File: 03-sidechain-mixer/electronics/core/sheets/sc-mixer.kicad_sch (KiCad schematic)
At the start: 48 parts, among them Q1 BC847BS, U1 TL072, U2 TL072, U3 TL072, U4 TL072

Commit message: Started VCF
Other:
- note added: "Pots to be moved over to the UI board"
- note added: "Pots to be moved over to the UI board. For channel 4 there can be two inputs from the UI board: one straigth from the jack (goes to peak detector), and one which is after a log volume pot control."
- note added: "Pots to be moved over to the UI board. The main volume control can happen on the UI board?"
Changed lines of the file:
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@@
+		)
+	)
+	(text "Pots to be moved over \nto the UI board.\nThe main volume control can\nhappen on the UI board?"
+		(exclude_from_sim no)
+		(at 287.02 63.5 0)
+		(effects
+			(font
+				(size 2 2)
+				(color 255 0 255 1)
+			)
+			(justify left)
 		)
 	)
@@
 			(font
 				(size 1.27 1.27)
+			)
+			(justify left)
+		)
+	)
+	(text "Pots to be moved over \nto the UI board"
+		(exclude_from_sim no)
+		(at 143.51 113.03 0)
+		(effects
+			(font
+				(size 2 2)
+				(color 255 0 255 1)
 			)
 			(justify left)
@@
 		)
 	)
+	(text "Pots to be moved over \nto the UI board.\nFor channel 4 there\ncan be two inputs from\nthe UI board: one straigth\nfrom the jack (goes to peak\ndetector), and one which is\nafter a log volume pot control.\n"
+		(exclude_from_sim no)
+		(at 40.64 186.69 0)
+		(effects
+			(font
+				(size 2 2)
+				(color 255 0 255 1)
+			)
+			(justify left)
+		)
+	)
 	(text "DC coupled input allows the mixer\nto be used for audio as well as CV"
 		(exclude_from_sim no)
@@
 			)
 			(justify left)
+		)
+	)
+	(text "Pots to be moved over \nto the UI board"
+		(exclude_from_sim no)
+		(at -7.62 55.88 0)
+		(effects
+			(font
+				(size 2 2)
+				(color 255 0 255 1)
+			)
+			(justify left)

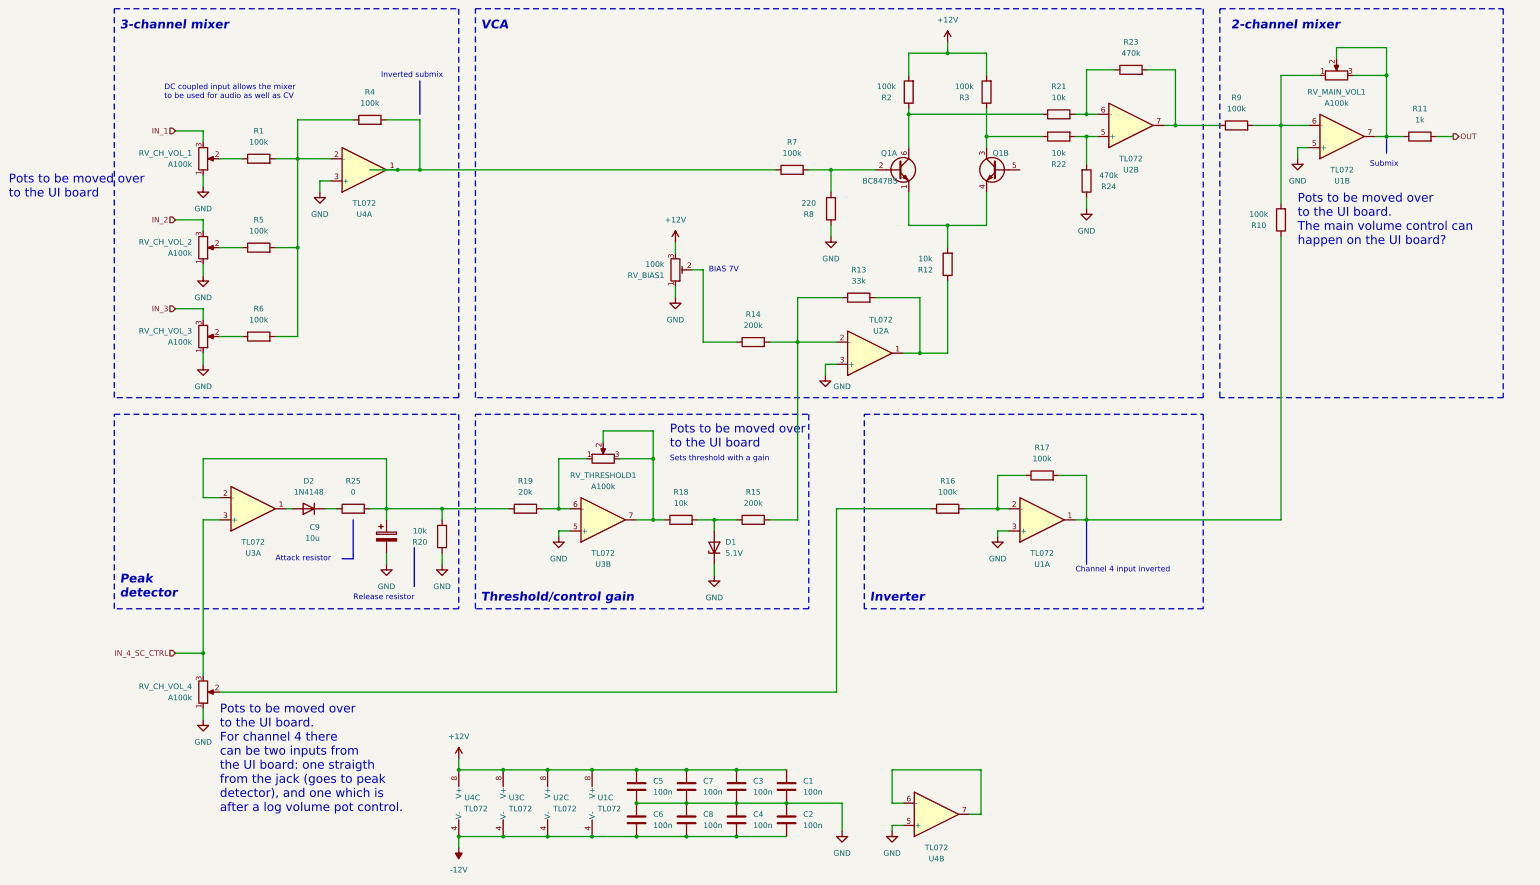
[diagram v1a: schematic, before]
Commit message: Updated sidechain mixer
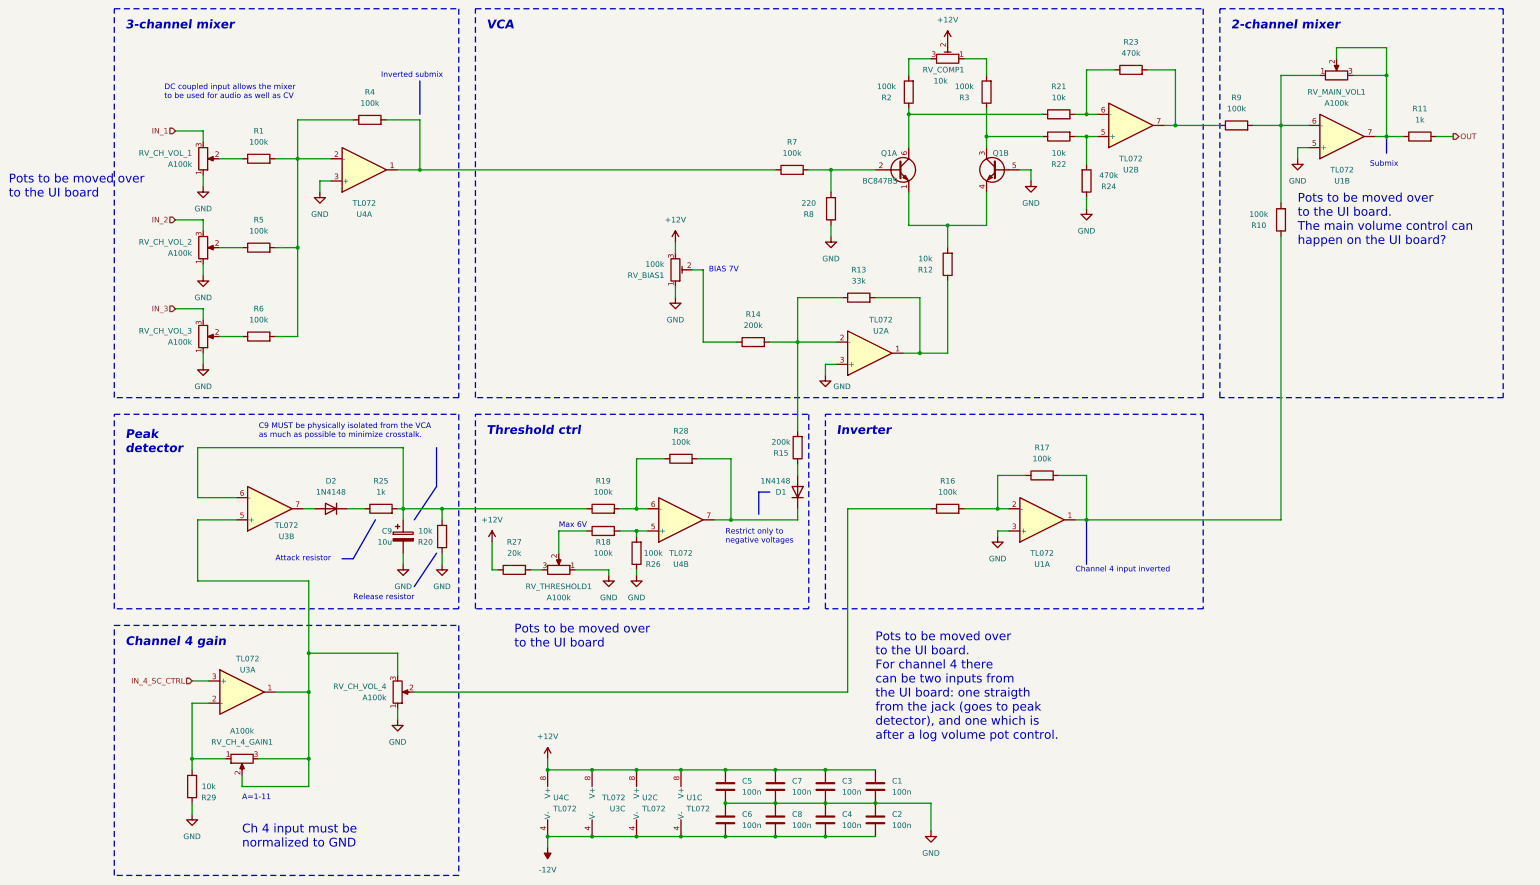
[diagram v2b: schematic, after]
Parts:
- removed D1: 5.1V, symbol Device:D_Zener
- added D1: 1N4148, symbol Device:D
- added R26, R28: 100k, Resistor_SMD:R_0603_1608Metric, symbol Device:R
- added R27: 20k, Resistor_SMD:R_0603_1608Metric, symbol Device:R
- added R29: 10k, Resistor_SMD:R_0603_1608Metric, symbol Device:R
- added RV_COMP1: 10k, symbol Device:R_Potentiometer_Trim
- added RV_THRESHOLD1: A100k, symbol Device:R_Potentiometer
- R18: value 10k -> 100k
- R19: value 20k -> 100k
- R25: value 0 -> 1k
- U3: footprint Package_SO:SOIC-8_3.9x4.9mm_P1.27mm -> (none); LCSC C6961 -> (none); Vendor JLCPCB -> (none)
- renumbered RV_THRESHOLD1 to RV_CH_4_GAIN1
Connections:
- net +12V: now also R27.1, RV_COMP1.2; no longer R2.2, R3.2
- net GND: now also Q1.5 (B2), R26.1, R29.1, RV_THRESHOLD1.1; no longer U3.5 (+), U4.5 (+)
- net IN_4_SC_CTRL: no longer RV_CH_VOL_4.3
- net at RV_CH_4_GAIN1.2, RV_CH_4_GAIN1.3: now also RV_CH_VOL_4.3, U3.1, U3.5 (+); no longer R18.1, U3.7
- net at U4.6 (-): now also R19.2, R28.1; no longer U4.7
- net at C9.1, R19.1, R20.2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: now also U3.6 (-); no longer U3.2 (-)
- net at R18.2: now also U4.5 (+), R26.2; no longer R15.1
- net at D2.2 (A): now also U3.7; no longer U3.1
- new net: D1.1 (K), R28.2, U4.7
- new net: R29.2, RV_CH_4_GAIN1.1, U3.2 (-)
- new net: R18.1, RV_THRESHOLD1.2
- new net: R27.2, RV_THRESHOLD1.3
- new net: R2.2, RV_COMP1.3
- new net: R3.2, RV_COMP1.1
- new net: D1.2 (A), R15.1
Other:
- note added: "A=1-11"
- note added: "C9 MUST be physically isolated from the VCA as much as possible to minimize crosstalk."
- note added: "Ch 4 input must be normalized to GND"
- note added: "Channel 4 gain"
- note added: "Max 6V"
- note added: "Restrict only to negative voltages"
- note added: "Threshold ctrl"
- note removed: "Sets threshold with a gain"
- note removed: "Threshold/control gain"
- moved on the sheet: C1, C2, C3, C4, C5, C6, C7, C8, C9, D2, R19, R25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

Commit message: Updated sidechain mixer schematics
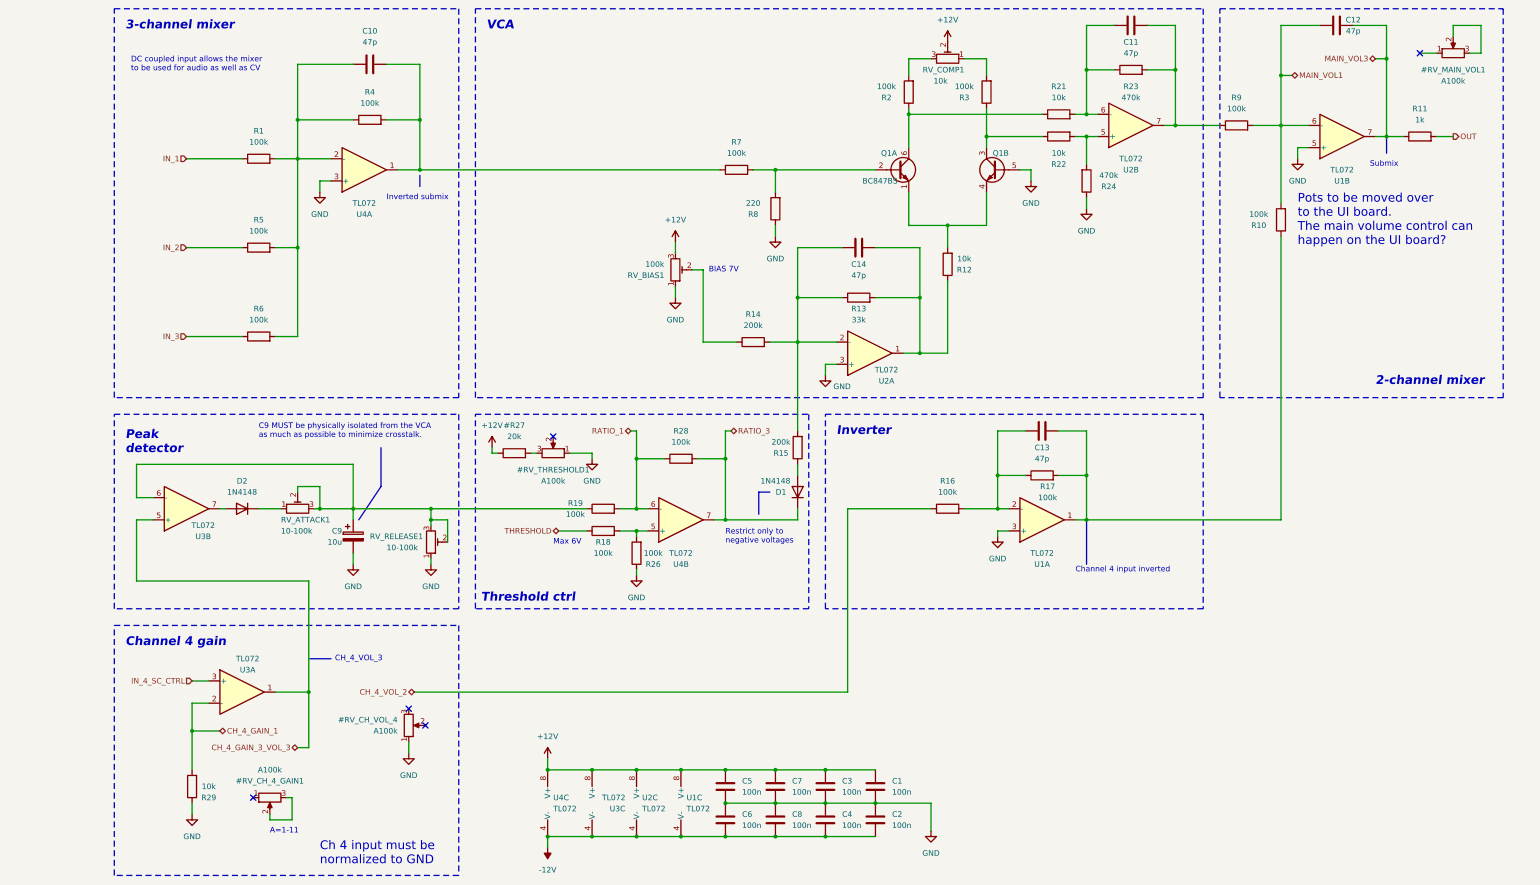
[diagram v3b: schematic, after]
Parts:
- removed R20: 10k, Resistor_SMD:R_0603_1608Metric, symbol Device:R
- removed R25: 1k, Resistor_SMD:R_0603_1608Metric, symbol Device:R
- removed RV_CH_VOL_1, RV_CH_VOL_2, RV_CH_VOL_3: A100k, symbol Device:R_Potentiometer
- added C10, C11, C12, C13, C14: 47p, Capacitor_SMD:C_0603_1608Metric_Pad1.08x0.95mm_HandSolder, symbol Device:C
- added RV_ATTACK1, RV_RELEASE1: 10-100k, symbol Device:R_Potentiometer_Trim
- R18, R19, R26, R29: footprint Resistor_SMD:R_0603_1608Metric -> Shmoergh_Custom_Footprints:R_Axial_DIN0207_L6.3mm_D2.5mm_P7.62mm_Horizontal; CHECKED YES -> (none); Vendor JLCPCB -> (none)
- R28: CHECKED YES -> (none); Vendor JLCPCB -> (none)
- renumbered R27 to #R27, RV_CH_4_GAIN1 to #RV_CH_4_GAIN1, RV_CH_VOL_4 to #RV_CH_VOL_4, RV_MAIN_VOL1 to #RV_MAIN_VOL1, RV_THRESHOLD1 to #RV_THRESHOLD1
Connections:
- net GND: now also RV_RELEASE1.1
- net IN_1: now also R1.1
- net IN_2: now also R5.1
- net IN_3: now also R6.1
- net MAIN_VOL1: now reaches R10.2, R9.2, U1.6 (-)
- net MAIN_VOL1: now also C12.1; no longer #RV_MAIN_VOL1.1
- net at #RV_MAIN_VOL1.2, #RV_MAIN_VOL1.3: no longer R11.1, U1.7
- net RATIO_1: now reaches R19.2, R28.1, U4.6 (-)
- net RATIO_3: now reaches D1.1 (K), R28.2, U4.7
- net CH_4_GAIN_1: now reaches R29.2, U3.2 (-)
- net CH_4_GAIN_1: no longer #RV_CH_4_GAIN1.1
- net at #RV_THRESHOLD1.2: no longer R18.1
- net at #RV_CH_VOL_4.2: no longer R16.1
- net at R4.2, R7.1, U4.1: now also C10.2
- net at R1.2, R4.1, R5.2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: now also C10.1
- net at R12.1, R13.2, U2.1: now also C14.2
- net at R16.2, R17.1, U1.2 (-): now also C13.1
- net at R10.1, R17.2, U1.1: now also C13.2
- net at C9.1, R19.1, U3.6 (-): now also RV_ATTACK1.2, RV_ATTACK1.3, RV_RELEASE1.2, RV_RELEASE1.3
- net at R21.2, R23.1, U2.6 (-): now also C11.1
- net at R23.2, R9.1, U2.7: now also C11.2
- net at D2.1 (K): now also RV_ATTACK1.1
- net at R13.1, R14.2, R15.2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: now also C14.1
- new net: #RV_CH_4_GAIN1.2, #RV_CH_4_GAIN1.3
- new net CH_4_GAIN_3_VOL_3: U3.1, U3.5 (+)
- new net CH_4_VOL_2: R16.1
- new net MAIN_VOL3: C12.2, R11.1, U1.7
- new net THRESHOLD: R18.1
- now unconnected: #RV_CH_VOL_4.3
- no-connect marks 0 -> 5
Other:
- note added: "CH_4_VOL_3"
- note removed: "Attack resistor"
- note removed: "Pots to be moved over to the UI board"
- note removed: "Pots to be moved over to the UI board. For channel 4 there can be two inputs from the UI board: one straigth from the jack (goes to peak detector), and one which is after a log volume pot control."
- note removed: "Release resistor"
- moved on the sheet: C9, D2, R7, R8, U3B

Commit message: Prepared sidechain mixer PCB
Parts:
- C1, C2, C3, C4, C5, C6, C7, C8, R1, R10, R16, R17, R2, R3, R4, R5, R6, R7, R9: CHECKED YES -> (none)
- C10, C11, C12, C13, C14: LCSC (none) -> C1671; Vendor (none) -> JLCPCB
- C9: footprint (none) -> Capacitor_SMD:CP_Elec_4x5.4; LCSC (none) -> C72485; Vendor (none) -> JLCPCB
- D1, D2: footprint (none) -> Diode_SMD:D_SOD-323; LCSC (none) -> C2128
- R11: CHECKED YES -> (none); LCSC (none) -> C21190
- R12, R21, R22: CHECKED YES -> (none); LCSC (none) -> C25804
- R13: CHECKED YES -> (none); LCSC (none) -> C4216
- R14, R15: CHECKED YES -> (none); LCSC (none) -> C25811
- R23, R24: CHECKED YES -> (none); LCSC (none) -> C23178
- R28: LCSC (none) -> C25803; Vendor (none) -> JLCPCB
- R8: CHECKED YES -> (none); LCSC (none) -> C22962
- RV_ATTACK1, RV_BIAS1, RV_COMP1, RV_RELEASE1: footprint (none) -> Potentiometer_THT:Potentiometer_ACP_CA6-H2,5_Horizontal
- U3: footprint (none) -> Package_SO:SOIC-8_3.9x4.9mm_P1.27mm; LCSC (none) -> C6961; Vendor (none) -> JLCPCB

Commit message: SC-Mixer PCB base done
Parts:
- D1, D2: footprint Diode_SMD:D_SOD-323 -> Diode_SMD:D_SOD-323_HandSoldering
- R28: footprint Resistor_SMD:R_0603_1608Metric -> Shmoergh_Custom_Footprints:R_Axial_DIN0207_L6.3mm_D2.5mm_P7.62mm_Horizontal; LCSC C25803 -> (none); Vendor JLCPCB -> (none)
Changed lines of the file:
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@@
 			)
 		)
-		(property "Footprint" "Resistor_SMD:R_0603_1608Metric"
+		(property "Footprint" "Shmoergh_Custom_Footprints:R_Axial_DIN0207_L6.3mm_D2.5mm_P7.62mm_Horizontal"
 			(at 146.05 119.888 90)
 			(effects
@@
 			)
 		)
-		(property "LCSC" "C25803"
+		(property "LCSC" ""
 			(at 146.05 118.11 90)
 			(effects
@@
 			)
 		)
-		(property "Vendor" "JLCPCB"
+		(property "Vendor" ""
 			(at 146.05 118.11 90)
 			(effects
@@
 			)
 		)
-		(property "Footprint" "Diode_SMD:D_SOD-323"
+		(property "Footprint" "Diode_SMD:D_SOD-323_HandSoldering"
 			(at 45.72 129.54 0)
 			(effects
@@
 			)
 		)
+		(property "Part No." ""
+			(at 45.72 129.54 0)
+			(effects
+				(font
+					(size 1.27 1.27)
+				)
+				(hide yes)
+			)
+		)
+		(property "Part URL" ""
+			(at 45.72 129.54 0)
+			(effects
+				(font
+					(size 1.27 1.27)
+				)
+				(hide yes)
+			)
+		)
+		(property "Vendor" ""
+			(at 45.72 129.54 0)
+			(effects
+				(font
+					(size 1.27 1.27)
+				)
+				(hide yes)
+			)
+		)
 		(pin "1"
 		)
@@
 			)
 		)
-		(property "Footprint" "Diode_SMD:D_SOD-323"
+		(property "Footprint" "Diode_SMD:D_SOD-323_HandSoldering"
 			(at 172.72 125.73 0)
 			(effects
@@
 			(effects
 				(font
+					(size 1.27 1.27)
+				)
+				(hide yes)
+			)
+		)
+		(property "Part No." ""
+			(at 172.72 125.73 0)
+			(effects
+				(font
+					(size 1.27 1.27)
+				)
+				(hide yes)
+			)
+		)
+		(property "Part URL" ""
+			(at 172.72 125.73 0)
+			(effects
+				(font
+					(size 1.27 1.27)
+				)
+				(hide yes)
+			)
+		)
+		(property "Vendor" ""
+			(at 172.72 125.73 0)
+			(effects
+				(font
